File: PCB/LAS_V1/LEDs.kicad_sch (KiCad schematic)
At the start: 4 parts

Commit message: installing JLB, PCB mostly done
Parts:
- removed D5: WS2813, LED_SMD:LED_WS2812_PLCC6_5.0x5.0mm_P1.6mm, symbol LED:WS2813
- added D2: WS2812B, LED_SMD:LED_WS2812B_PLCC4_5.0x5.0mm_P3.2mm, symbol LED:WS2812B
- added R11: 0, symbol Device:R_Small_US
- added R11 (x3): 1.2k, symbol Device:R_Small_US
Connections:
- net GND: now also D2.3 (VSS)
- net GREEN: now also R11.1; no longer D8.2 (A)
- net RED: now also R11.1; no longer D6.2 (A)
- net YELLOW: now also R11.1; no longer D7.2 (A)
- new net: D2.1 (VDD), R11.2
- new net: D7.2 (A), R11.2
- new net: D8.2 (A), R11.2
- new net: D6.2 (A), R11.2
- new net +5V: R11.1
- new net DIN: D2.4 (DIN)
- no-connect marks 0 -> 1

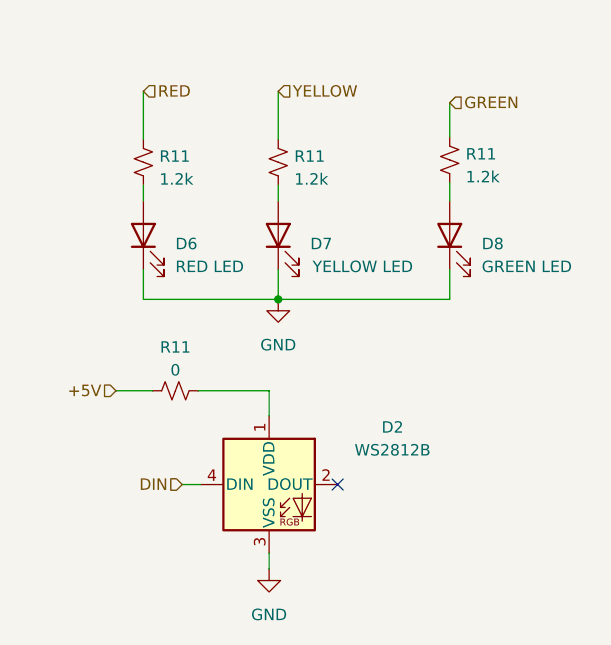
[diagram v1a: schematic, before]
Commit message: added JLBPCB part Numbers
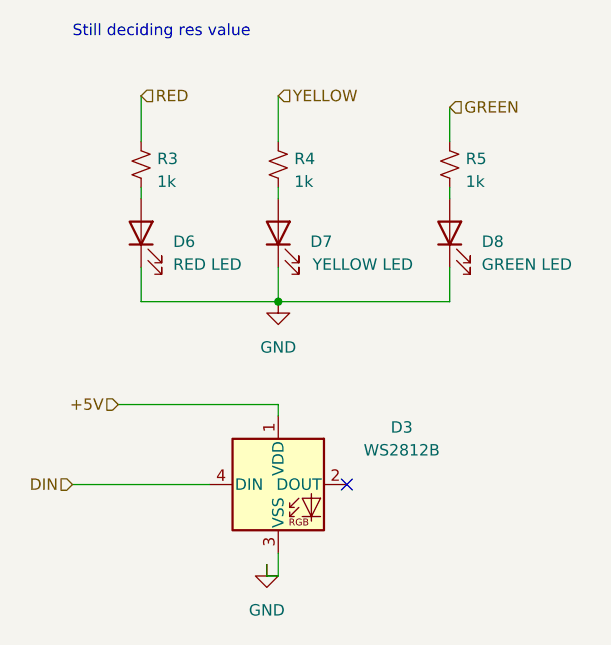
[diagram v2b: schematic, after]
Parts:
- removed R11: 0, symbol Device:R_Small_US
- D3: renamed from D2; LCSC (none) -> C2843785
- D6: footprint (none) -> LED_SMD:LED_0603_1608Metric; LCSC (none) -> C2286
- D7: footprint (none) -> LED_SMD:LED_0805_2012Metric; LCSC (none) -> C2296
- D8: footprint (none) -> LED_SMD:LED_0805_2012Metric; LCSC (none) -> C2297
- R3, R4, R5: renamed from R11; value 1.2k -> 1k; footprint (none) -> Resistor_SMD:R_0603_1608Metric; LCSC (none) -> C21190
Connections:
- net +5V: now also D3.1 (VDD)
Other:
- note added: "Still deciding res value"
- moved on the sheet: D3, R5

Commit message: All components Placed on PCB
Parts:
- D6: footprint LED_SMD:LED_0603_1608Metric -> LED_SMD:LED_0805_2012Metric; LCSC C2286 -> C84256
- renumbered D3 to D4, R3 to R5, R4 to R6, R5 to R7
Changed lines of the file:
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@@
   (symbol (lib_id "Device:R_Small_US") (at 140.97 81.28 0) (unit 1)
     (in_bom yes) (on_board yes) (dnp no) (fields_autoplaced)
-    (property "Reference" "R4" (at 142.748 80.645 0)
+    (property "Reference" "R6" (at 142.748 80.645 0)
       (effects (font (size 1.27 1.27)) (justify left))
     )
@@
       (project "LAS_V1"
         (path "/aadef4b8-3115-4a49-998f-828f2021a6b4/f48c28f3-4e7e-4446-924c-0b87434ade9c"
-          (reference "R4") (unit 1)
+          (reference "R6") (unit 1)
         )
       )
@@
         )
         (path "/aadef4b8-3115-4a49-998f-828f2021a6b4/f48c28f3-4e7e-4446-924c-0b87434ade9c"
+          (reference "#PWR017") (unit 1)
+        )
+      )
+    )
+  )
+  (symbol (lib_id "power:GND") (at 139.7 125.73 0) (unit 1)
+    (in_bom yes) (on_board yes) (dnp no) (fields_autoplaced)
+    (property "Reference" "#PWR021" (at 139.7 132.08 0)
+      (effects (font (size 1.27 1.27)) hide)
+    )
+    (property "Value" "GND" (at 139.7 130.81 0)
+      (effects (font (size 1.27 1.27)))
+    )
+    (property "Footprint" "" (at 139.7 125.73 0)
+      (effects (font (size 1.27 1.27)) hide)
+    )
+    (property "Datasheet" "" (at 139.7 125.73 0)
+      (effects (font (size 1.27 1.27)) hide)
+    )
+    (pin "1")
+    (instances
+      (project "LAS_V1"
+        (path "/aadef4b8-3115-4a49-998f-828f2021a6b4"
+          (reference "#PWR021") (unit 1)
+        )
+        (path "/aadef4b8-3115-4a49-998f-828f2021a6b4/f48c28f3-4e7e-4446-924c-0b87434ade9c"
           (reference "#PWR016") (unit 1)
         )
@@
     )
   )
-  (symbol (lib_id "power:GND") (at 139.7 125.73 0) (unit 1)
-    (in_bom yes) (on_board yes) (dnp no) (fields_autoplaced)
-    (property "Reference" "#PWR021" (at 139.7 132.08 0)
-      (effects (font (size 1.27 1.27)) hide)
-    )
-    (property "Value" "GND" (at 139.7 130.81 0)
-      (effects (font (size 1.27 1.27)))
-    )
-    (property "Footprint" "" (at 139.7 125.73 0)
-      (effects (font (size 1.27 1.27)) hide)
-    )
-    (property "Datasheet" "" (at 139.7 125.73 0)
-      (effects (font (size 1.27 1.27)) hide)
-    )
-    (pin "1")
-    (instances
-      (project "LAS_V1"
-        (path "/aadef4b8-3115-4a49-998f-828f2021a6b4"
-          (reference "#PWR021") (unit 1)
-        )
-        (path "/aadef4b8-3115-4a49-998f-828f2021a6b4/f48c28f3-4e7e-4446-924c-0b87434ade9c"
-          (reference "#PWR015") (unit 1)
-        )
-      )
-    )
-  )
   (symbol (lib_id "Device:LED") (at 160.02 88.9 90) (unit 1)
     (in_bom yes) (on_board yes) (dnp no) (fields_autoplaced)
@@
         )
         (path "/aadef4b8-3115-4a49-998f-828f2021a6b4/f48c28f3-4e7e-4446-924c-0b87434ade9c"
-          (reference "D4") (unit 1)
+          (reference "D5") (unit 1)
         )
       )
@@
   (symbol (lib_id "LED:WS2812B") (at 140.97 116.84 0) (unit 1)
     (in_bom yes) (on_board yes) (dnp no)
-    (property "Reference" "D3" (at 154.686 110.49 0)
+    (property "Reference" "D4" (at 154.686 110.49 0)
       (effects (font (size 1.27 1.27)))
     )
@@
       (project "LAS_V1"
         (path "/aadef4b8-3115-4a49-998f-828f2021a6b4/f48c28f3-4e7e-4446-924c-0b87434ade9c"
-          (reference "D3") (unit 1)
+          (reference "D4") (unit 1)
         )
       )
@@
   (symbol (lib_id "Device:R_Small_US") (at 160.02 81.28 0) (unit 1)
     (in_bom yes) (on_board yes) (dnp no) (fields_autoplaced)
-    (property "Reference" "R5" (at 161.798 80.645 0)
+    (property "Reference" "R7" (at 161.798 80.645 0)
       (effects (font (size 1.27 1.27)) (justify left))
     )
@@
       (project "LAS_V1"
         (path "/aadef4b8-3115-4a49-998f-828f2021a6b4/f48c28f3-4e7e-4446-924c-0b87434ade9c"
+          (reference "R7") (unit 1)
+        )
+      )
+    )
+  )
+  (symbol (lib_id "Device:R_Small_US") (at 125.73 81.28 0) (unit 1)
+    (in_bom yes) (on_board yes) (dnp no) (fields_autoplaced)
+    (property "Reference" "R5" (at 127.508 80.645 0)
+      (effects (font (size 1.27 1.27)) (justify left))
+    )
+    (property "Value" "1k" (at 127.508 83.185 0)
+      (effects (font (size 1.27 1.27)) (justify left))
+    )
+    (property "Footprint" "Resistor_SMD:R_0603_1608Metric" (at 125.73 81.28 0)
+      (effects (font (size 1.27 1.27)) hide)
+    )
+    (property "Datasheet" "~" (at 125.73 81.28 0)
+      (effects (font (size 1.27 1.27)) hide)
+    )
+    (property "LCSC" "C21190" (at 125.73 81.28 0)
+      (effects (font (size 1.27 1.27)) hide)
+    )
+    (pin "1")
+    (pin "2")
+    (instances
+      (project "LAS_V1"
+        (path "/aadef4b8-3115-4a49-998f-828f2021a6b4/f48c28f3-4e7e-4446-924c-0b87434ade9c"
           (reference "R5") (unit 1)
         )
@@
     )
   )
-  (symbol (lib_id "Device:R_Small_US") (at 125.73 81.28 0) (unit 1)
-    (in_bom yes) (on_board yes) (dnp no) (fields_autoplaced)
-    (property "Reference" "R3" (at 127.508 80.645 0)
-      (effects (font (size 1.27 1.27)) (justify left))
-    )
-    (property "Value" "1k" (at 127.508 83.185 0)
-      (effects (font (size 1.27 1.27)) (justify left))
-    )
-    (property "Footprint" "Resistor_SMD:R_0603_1608Metric" (at 125.73 81.28 0)
-      (effects (font (size 1.27 1.27)) hide)
-    )
-    (property "Datasheet" "~" (at 125.73 81.28 0)
-      (effects (font (size 1.27 1.27)) hide)
-    )
-    (property "LCSC" "C21190" (at 125.73 81.28 0)
-      (effects (font (size 1.27 1.27)) hide)
-    )
-    (pin "1")
-    (pin "2")
-    (instances
-      (project "LAS_V1"
-        (path "/aadef4b8-3115-4a49-998f-828f2021a6b4/f48c28f3-4e7e-4446-924c-0b87434ade9c"
-          (reference "R3") (unit 1)
-        )
-      )
-    )
-  )
   (symbol (lib_id "Device:LED") (at 125.73 88.9 90) (unit 1)
     (in_bom yes) (on_board yes) (dnp no) (fields_autoplaced)
@@
       (effects (font (size 1.27 1.27)) (justify right))
     )
-    (property "Footprint" "LED_SMD:LED_0603_1608Metric" (at 125.73 88.9 0)
+    (property "Footprint" "LED_SMD:LED_0805_2012Metric" (at 125.73 88.9 0)
       (effects (font (size 1.27 1.27)) hide)
     )
@@
       (effects (font (size 1.27 1.27)) hide)
     )
-    (property "LCSC" "C2286" (at 125.73 88.9 0)
+    (property "LCSC" "C84256" (at 125.73 88.9 0)
       (effects (font (size 1.27 1.27)) hide)
     )
@@
         )
         (path "/aadef4b8-3115-4a49-998f-828f2021a6b4/f48c28f3-4e7e-4446-924c-0b87434ade9c"
-          (reference "D1") (unit 1)
+          (reference "D2") (unit 1)
         )
       )
@@
         )
         (path "/aadef4b8-3115-4a49-998f-828f2021a6b4/f48c28f3-4e7e-4446-924c-0b87434ade9c"
-          (reference "D2") (unit 1)
-        )
-      )
+          (reference "D3") (unit 1)
+        )
+      )
